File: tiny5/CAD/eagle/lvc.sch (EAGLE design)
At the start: 5 parts, among them U1 LT3007, U2 ATTINY5

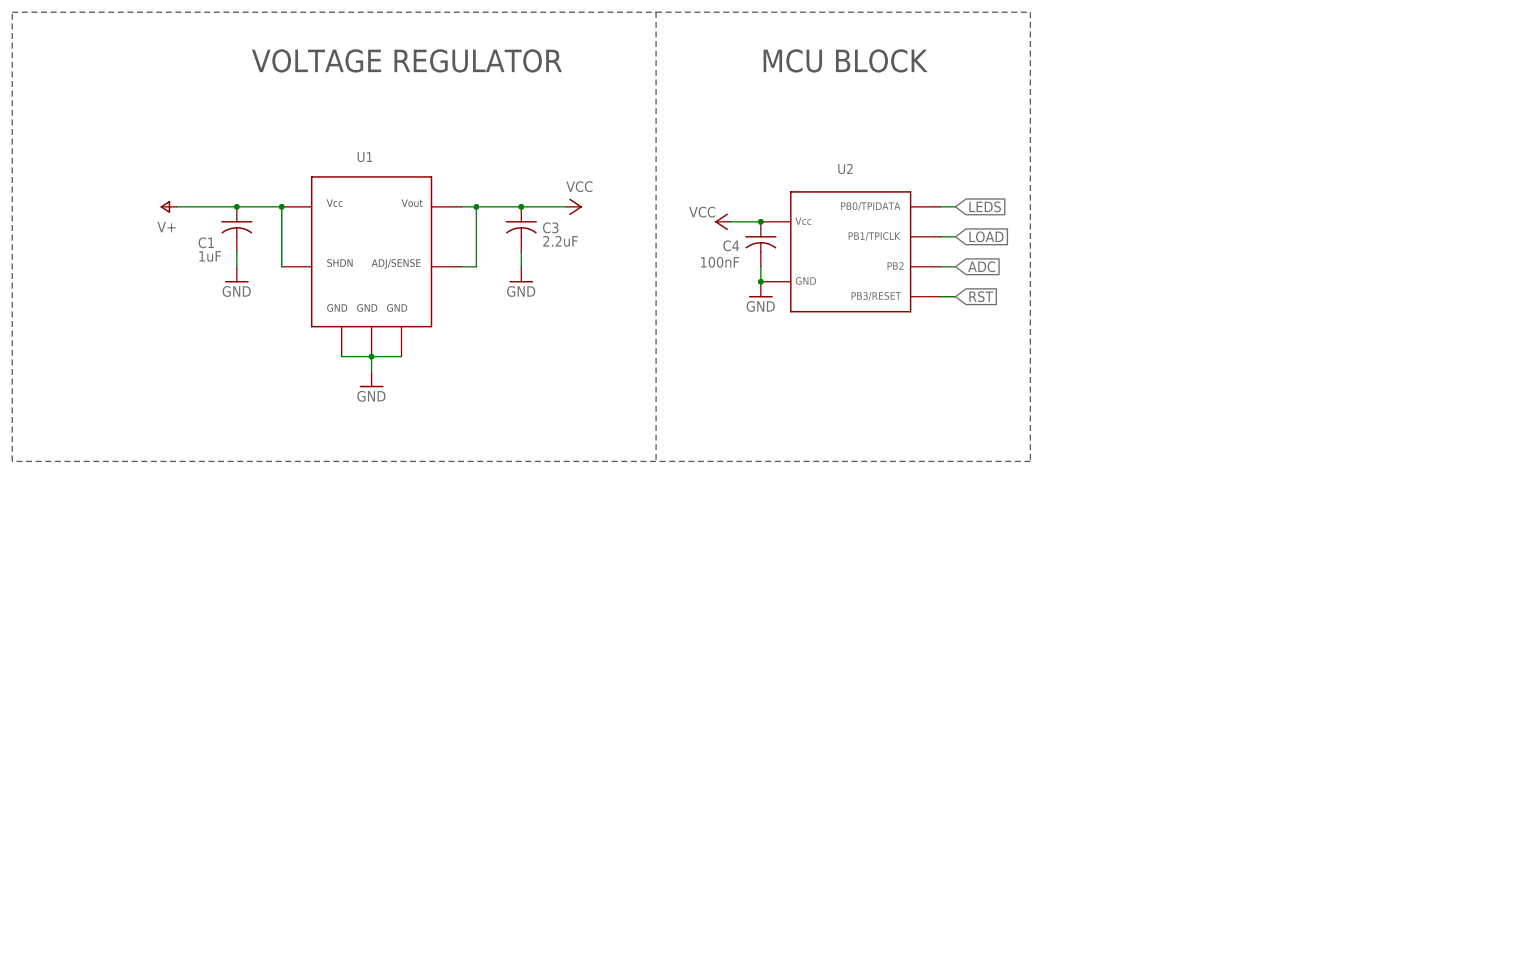
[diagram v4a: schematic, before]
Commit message: Started layout
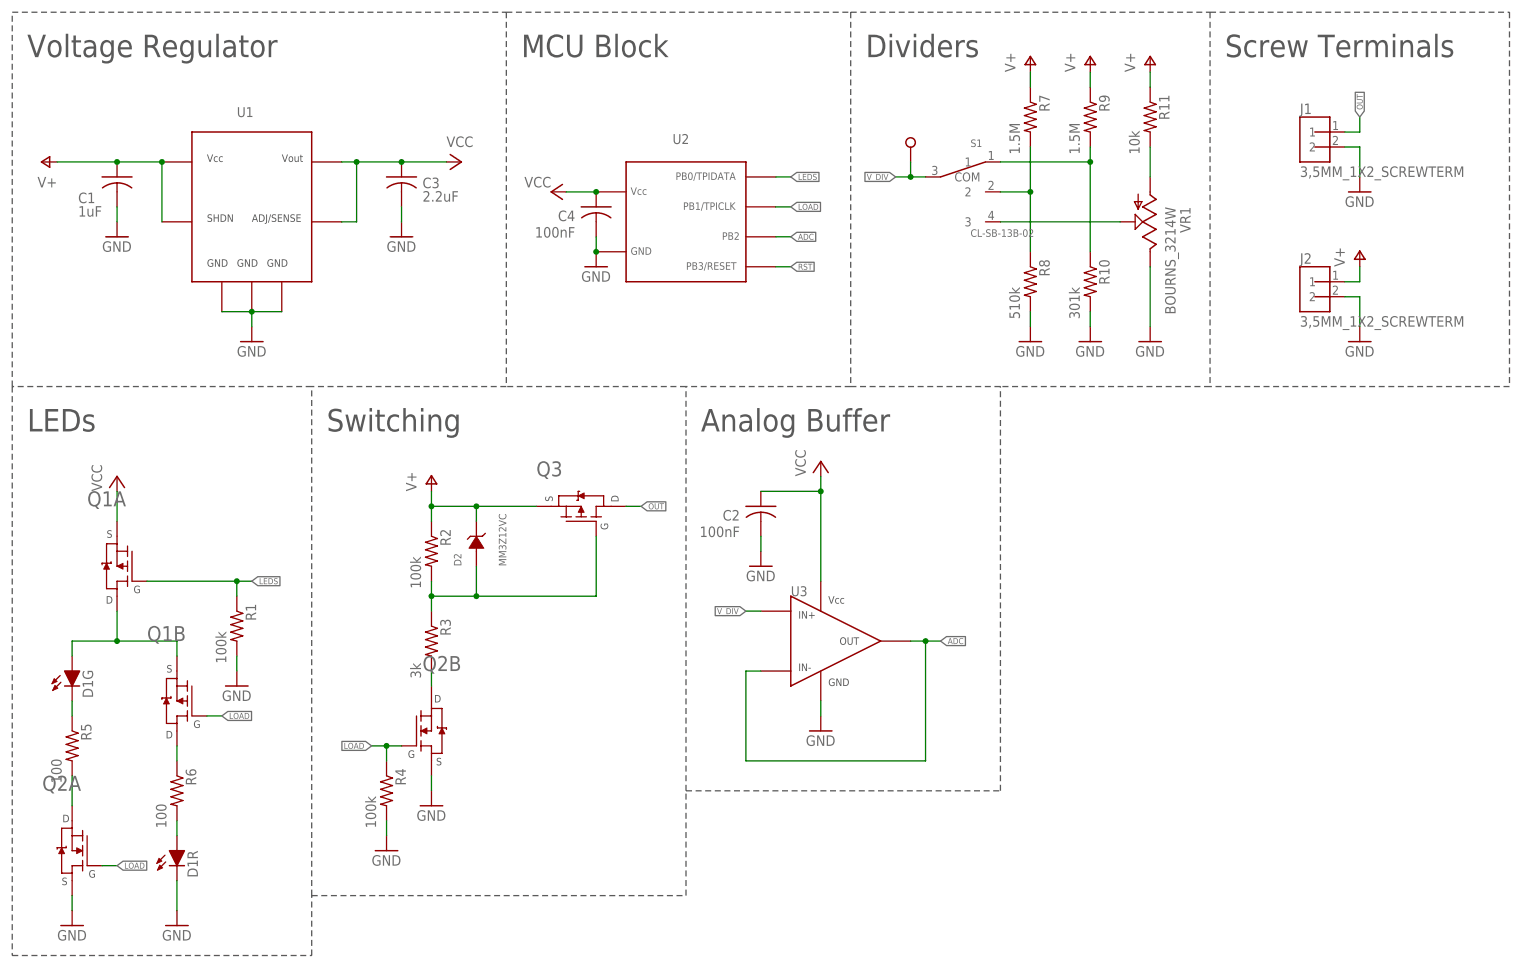
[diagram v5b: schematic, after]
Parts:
- added C2: 100nF, resistor:C-USC0603
- added D1: LED-R/G_150141RV73100, AR_led:LED-R/G_150141RV73100
- added D2: MM3Z12VC, NR_diode:MM3Z12VC
- added J1, J2: 3,5MM_1X2_SCREWTERM, NR_conn:3,5MM_1X2_SCREWTERM
- added Q1: FDC6312P, AR_transistor:FDC6312P
- added Q2: PMGD280UN, AR_transistor:PMGD280UN
- added Q3: SQJ463EP, AR_transistor:SQJ463EP
- added R1, R2, R4: 100k, resistor:R-US_R0603
- added R10: 301k, resistor:R-US_R0603
- added R11: 10k, resistor:R-US_R0603
- added R3: 3k, resistor:R-US_R0603
- added R5, R6: 100, resistor:R-US_R0603
- added R7, R9: 1.5M, resistor:R-US_R0603
- added R8: 510k, resistor:R-US_R0603
- added S1: CL-SB-13B-02, NR_switch:CL-SB-13B-02
- added TP1: TESTPOINT, CM_test:TESTPOINT
- added U3: LT1494, AR_op_amps:LT1494
- added VR1: BOURNS_3214W, NR_pot:BOURNS_3214W
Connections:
- new net 2_CELL: R7.2, R8.1, S1.2
- new net 3_CELL: R10.1, R9.2, S1.1
- new net ADJ: S1.3, VR1.S
- new net N$1: Q2A.D, R5.2
- new net N$11: R11.2, VR1.A
- new net N$2: D1G.C, R5.1
- new net N$3: D1G.A, Q1A.D, Q1B.S
- new net N$4: Q1B.D, R6.1
- new net N$5: D2.A, Q3.G, R2.2, R3.1
- new net N$6: D1R.A, R6.2
- new net N$7: Q2B.D, R3.2
- new net OUT: J1.1, Q3.D
- new net V_DIV: S1.COM, TP1.P$1, U3.IN+
- net ADC: now also U3.IN-, U3.OUT
- net GND: now also C2.2, D1R.C, J1.2, J2.2, Q2A.S, Q2B.S, R1.2, R10.2, R4.2, R8.2, U3.GND, VR1.E
- net LEDS: now also Q1A.G, R1.1
- net LOAD: now also Q1B.G, Q2A.G, Q2B.G, R4.1
- net V+: now also D2.C, J2.1, Q3.S, R11.1, R2.1, R7.1, R9.1
- net VCC: now also C2.1, Q1A.S, U3.VCC
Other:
- note added: "Analog Buffer"
- note added: "Dividers"
- note added: "LEDs"
- note added: "MCU Block"
- note added: "Screw Terminals"
- note added: "Switching"
- note added: "Voltage Regulator"
- note removed: "MCU BLOCK"
- note removed: "VOLTAGE REGULATOR"
- moved on the sheet: C1, C3, C4, U1, U2

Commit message: Finished routing
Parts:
- added J3: 2X3_50MIL, NR_conn:2X3_50MIL
- added JP1: (no value), pinhead:PINHD-1X2
- added R12: 100k, resistor:R-US_R0603
- added S2: CL-SB-12B-02, AR_switches:CL-SB-12B-02
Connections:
- net N$6 renamed RA
- new net EN: JP1.2, R12.1, S2.P$1, U1.SHDN
- net GND: now also J1.1, J3.6, R12.2; no longer J1.2
- net LEDS: now also J3.1
- net LOAD: now also J3.3
- net OUT: now also J1.2; no longer J1.1
- net RST: now also J3.5
- net V+: now also JP1.1, S2.P$2; no longer U1.SHDN
- net VCC: now also J3.2
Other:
- note added: "TPI"
- moved on the sheet: C1, J1

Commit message: Prettified schematic
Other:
- note added: "On Switch"
- moved on the sheet: JP1, R12, S2
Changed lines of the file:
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@@
 <wire x1="175.26" y1="109.22" x2="210.82" y2="109.22" width="0.1524" layer="97" style="shortdash"/>
 <wire x1="210.82" y1="109.22" x2="210.82" y2="144.78" width="0.1524" layer="97" style="shortdash"/>
+<wire x1="210.82" y1="109.22" x2="261.62" y2="109.22" width="0.1524" layer="97" style="shortdash"/>
+<wire x1="261.62" y1="109.22" x2="261.62" y2="144.78" width="0.1524" layer="97" style="shortdash"/>
+<text x="213.36" y="139.7" size="3.81" layer="97">On Switch</text>
 </plain>
 <instances>
@@
 </instance>
 <instance part="GND17" gate="1" x="203.2" y="114.3"/>
-<instance part="R12" gate="G$1" x="220.98" y="127" rot="R270"/>
-<instance part="GND18" gate="1" x="220.98" y="116.84"/>
-<instance part="P+12" gate="1" x="246.38" y="142.24"/>
-<instance part="S2" gate="G$1" x="233.68" y="134.62"/>
-<instance part="JP1" gate="G$1" x="233.68" y="119.38" rot="R270"/>
+<instance part="R12" gate="G$1" x="231.14" y="124.46" rot="R270"/>
+<instance part="GND18" gate="1" x="231.14" y="114.3"/>
+<instance part="P+12" gate="1" x="256.54" y="139.7"/>
+<instance part="S2" gate="G$1" x="243.84" y="132.08"/>
+<instance part="JP1" gate="G$1" x="243.84" y="116.84" rot="R270"/>
 </instances>
 <busses>
@@
 <pinref part="R12" gate="G$1" pin="2"/>
 <pinref part="GND18" gate="1" pin="GND"/>
-<wire x1="220.98" y1="121.92" x2="220.98" y2="119.38" width="0.1524" layer="91"/>
+<wire x1="231.14" y1="119.38" x2="231.14" y2="116.84" width="0.1524" layer="91"/>
 </segment>
 </net>
@@
 <segment>
 <pinref part="P+12" gate="1" pin="V+"/>
-<wire x1="246.38" y1="139.7" x2="246.38" y2="137.16" width="0.1524" layer="91"/>
+<wire x1="256.54" y1="137.16" x2="256.54" y2="134.62" width="0.1524" layer="91"/>
 <pinref part="S2" gate="G$1" pin="P$2"/>
-<wire x1="246.38" y1="137.16" x2="243.84" y2="137.16" width="0.1524" layer="91"/>
+<wire x1="256.54" y1="134.62" x2="254" y2="134.62" width="0.1524" layer="91"/>
 <pinref part="JP1" gate="G$1" pin="1"/>
-<wire x1="243.84" y1="137.16" x2="238.76" y2="137.16" width="0.1524" layer="91"/>
-<wire x1="236.22" y1="121.92" x2="236.22" y2="127" width="0.1524" layer="91"/>
-<wire x1="236.22" y1="127" x2="243.84" y2="127" width="0.1524" layer="91"/>
-<wire x1="243.84" y1="127" x2="243.84" y2="137.16" width="0.1524" layer="91"/>
-<junction x="243.84" y="137.16"/>
+<wire x1="254" y1="134.62" x2="248.92" y2="134.62" width="0.1524" layer="91"/>
+<wire x1="246.38" y1="119.38" x2="246.38" y2="124.46" width="0.1524" layer="91"/>
+<wire x1="246.38" y1="124.46" x2="254" y2="124.46" width="0.1524" layer="91"/>
+<wire x1="254" y1="124.46" x2="254" y2="134.62" width="0.1524" layer="91"/>
+<junction x="254" y="134.62"/>
 </segment>
 </net>
@@
 </segment>
 <segment>
-<wire x1="236.22" y1="187.96" x2="236.22" y2="190.5" width="0.1524" layer="91"/>
-<label x="236.22" y="190.5" size="1.016" layer="95" rot="R90" xref="yes"/>
+<wire x1="236.22" y1="187.96" x2="236.22" y2="193.04" width="0.1524" layer="91"/>
+<label x="236.22" y="193.04" size="1.016" layer="95" rot="R90" xref="yes"/>
 <pinref part="J1" gate="G$1" pin="2"/>
 <wire x1="238.76" y1="187.96" x2="236.22" y2="187.96" width="0.1524" layer="91"/>
@@
 <segment>
 <pinref part="R12" gate="G$1" pin="1"/>
-<wire x1="220.98" y1="132.08" x2="220.98" y2="134.62" width="0.1524" layer="91"/>
-<wire x1="220.98" y1="134.62" x2="218.44" y2="134.62" width="0.1524" layer="91"/>
-<junction x="220.98" y="134.62"/>
-<label x="218.44" y="134.62" size="1.016" layer="95" rot="R180" xref="yes"/>
+<wire x1="231.14" y1="129.54" x2="231.14" y2="132.08" width="0.1524" layer="91"/>
+<wire x1="231.14" y1="132.08" x2="228.6" y2="132.08" width="0.1524" layer="91"/>
+<junction x="231.14" y="132.08"/>
+<label x="228.6" y="132.08" size="1.016" layer="95" rot="R180" xref="yes"/>
 <pinref part="S2" gate="G$1" pin="P$1"/>
-<wire x1="228.6" y1="134.62" x2="226.06" y2="134.62" width="0.1524" layer="91"/>
+<wire x1="238.76" y1="132.08" x2="236.22" y2="132.08" width="0.1524" layer="91"/>
 <pinref part="JP1" gate="G$1" pin="2"/>
-<wire x1="226.06" y1="134.62" x2="220.98" y2="134.62" width="0.1524" layer="91"/>
-<wire x1="233.68" y1="121.92" x2="233.68" y2="127" width="0.1524" layer="91"/>
-<wire x1="233.68" y1="127" x2="226.06" y2="127" width="0.1524" layer="91"/>
-<wire x1="226.06" y1="127" x2="226.06" y2="134.62" width="0.1524" layer="91"/>
-<junction x="226.06" y="134.62"/>
-</segment>
-</net>
+<wire x1="236.22" y1="132.08" x2="231.14" y2="132.08" width="0.1524" layer="91"/>
+<wire x1="243.84" y1="119.38" x2="243.84" y2="124.46" width="0.1524" layer="91"/>
+<wire x1="243.84" y1="124.46" x2="236.22" y2="124.46" width="0.1524" layer="91"/>
+<wire x1="236.22" y1="124.46" x2="236.22" y2="132.08" width="0.1524" layer="91"/>
+<junction x="236.22" y="132.08"/>
+</segment>
+</net>

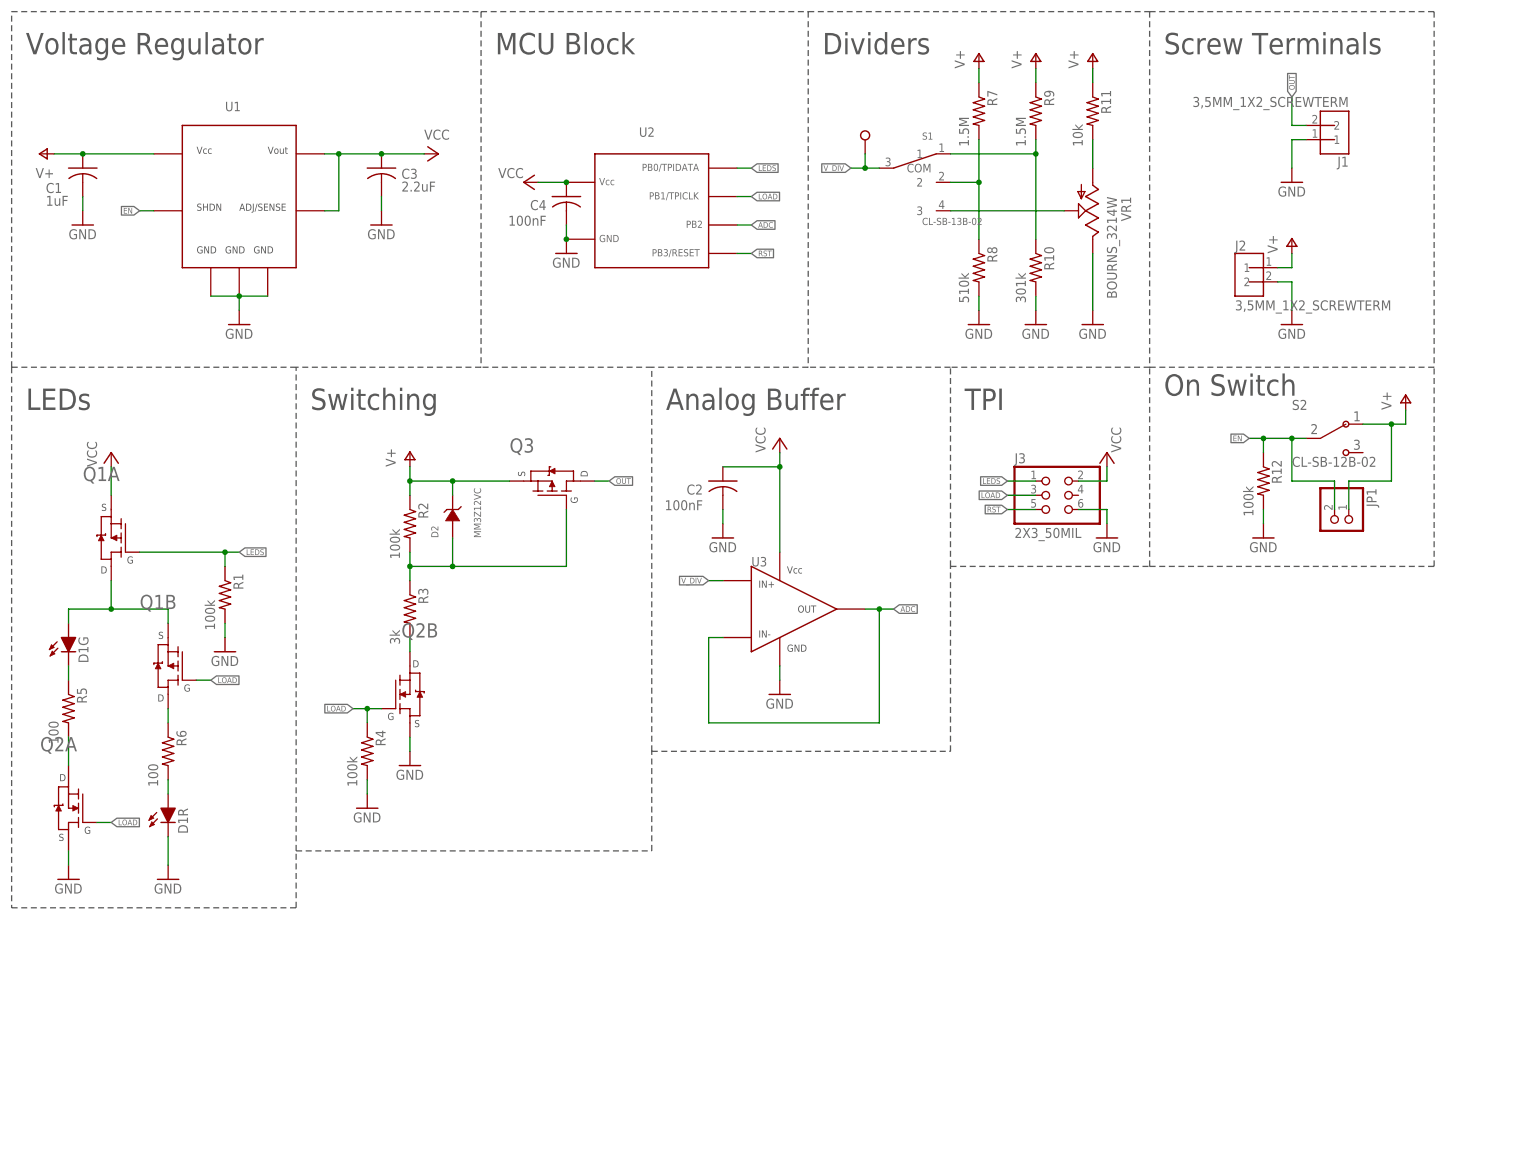
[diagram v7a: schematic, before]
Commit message: updated schematic for reverse polarity protection
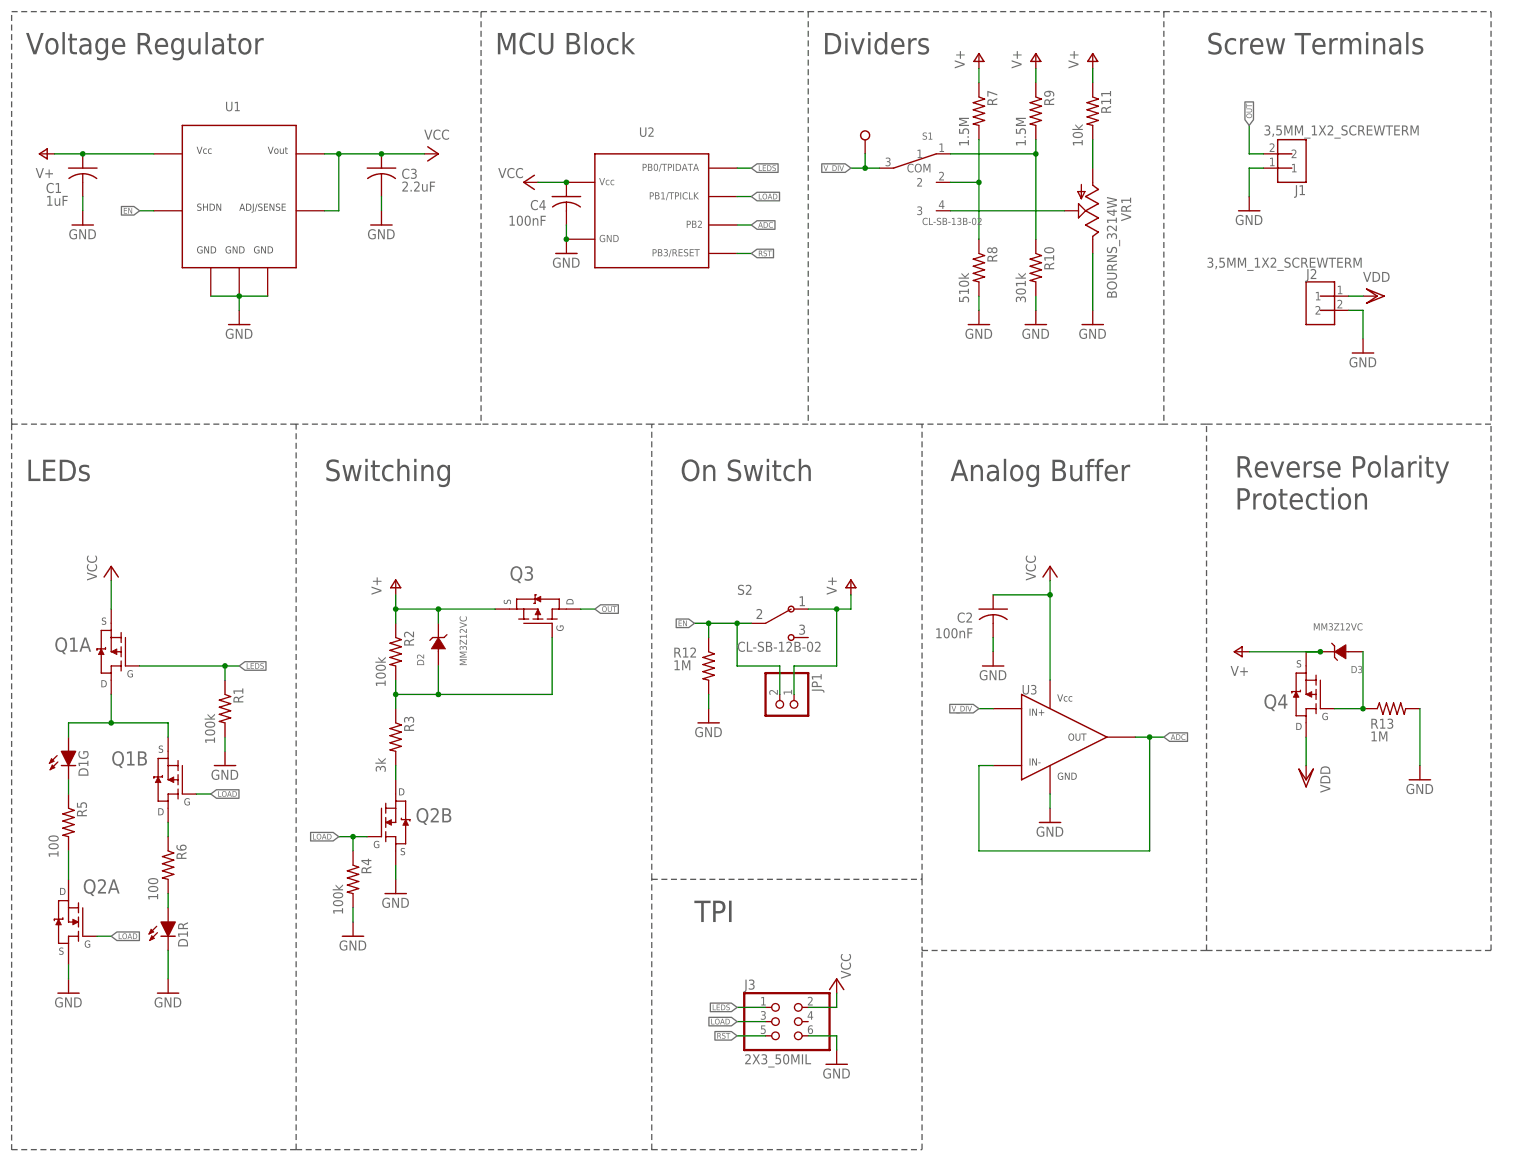
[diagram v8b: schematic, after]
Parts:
- added D3: MM3Z12VC, NR_diode:MM3Z12VC
- added Q4: DMP3010LPS, AR_transistor:DMP3010LPS
- added R13: 1M, resistor:R-US_R0603
- Q3: value SQJ463EP -> DMP3010LPS; device AR_transistor:SQJ463EP -> AR_transistor:DMP3010LPS
- R12: value 100k -> 1M
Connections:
- new net N$6: D3.A, Q4.G, R13.1
- new net VDD: J2.1, Q4.D
- net GND: now also R13.2
- net V+: now also D3.C, Q4.S; no longer J2.1
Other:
- note added: "Reverse Polarity Protection"
- moved on the sheet: C2, D1G, D1R, D2, J1, J2, J3, JP1, Q1A, Q1B, Q2A, Q2B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
